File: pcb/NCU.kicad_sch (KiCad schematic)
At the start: 0 parts

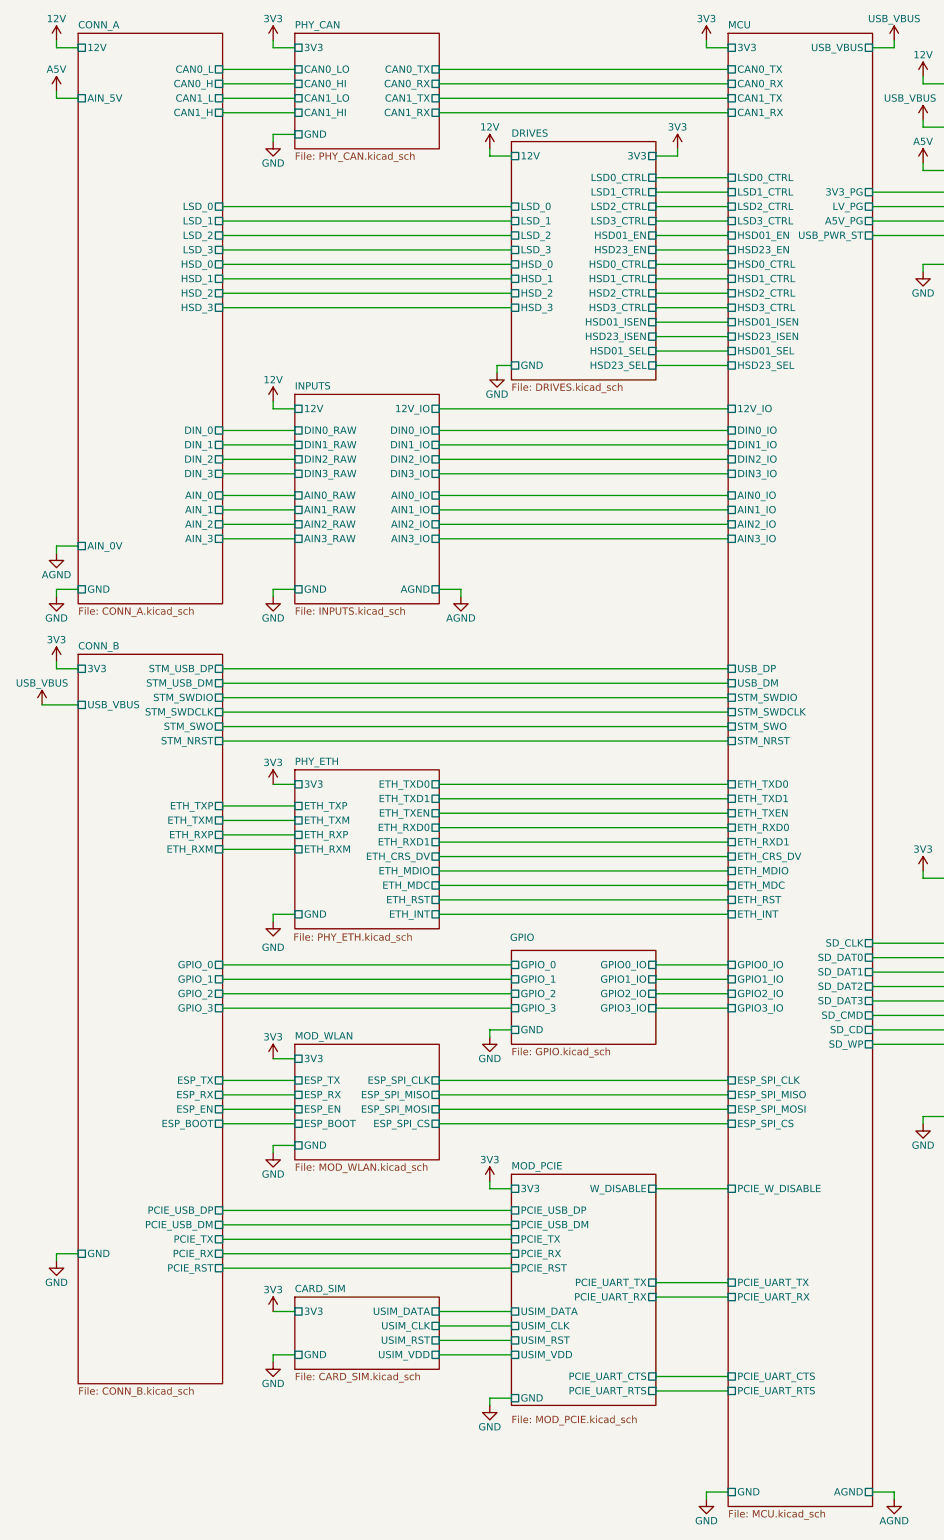
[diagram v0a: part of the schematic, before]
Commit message: added better lsds
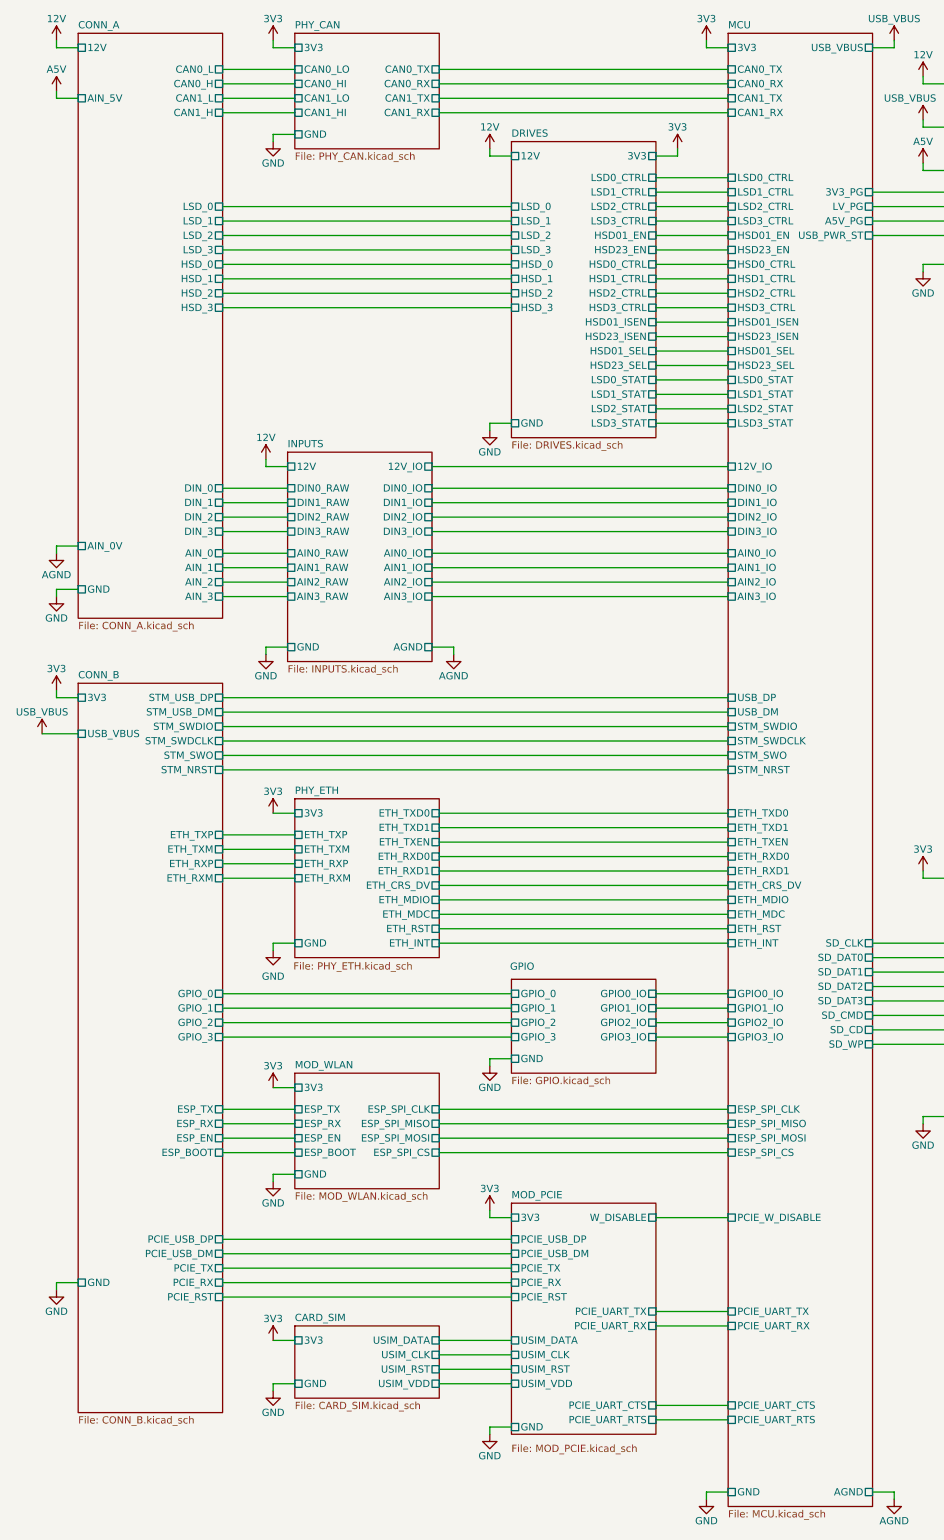
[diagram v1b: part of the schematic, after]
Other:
- sheet DRIVES ports: added LSD0_STAT, LSD1_STAT, LSD2_STAT, LSD3_STAT; removed none
- sheet MCU ports: added LSD0_STAT, LSD1_STAT, LSD2_STAT, LSD3_STAT; removed none

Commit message: power done
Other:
- sheet PWR ports: added 12V_PRT; removed none
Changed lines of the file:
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@@
 	(wire
 		(pts
+			(xy 208.28 26.67) (xy 208.28 27.94)
+		)
+		(stroke
+			(width 0)
+			(type default)
+		)
+	)
+	(wire
+		(pts
 			(xy 50.8 104.14) (xy 62.23 104.14)
 		)
@@
 	(wire
 		(pts
+			(xy 204.47 27.94) (xy 208.28 27.94)
+		)
+		(stroke
+			(width 0)
+			(type default)
+		)
+	)
+	(wire
+		(pts
 			(xy 165.1 52.07) (xy 177.8 52.07)
 		)
@@
 	(wire
 		(pts
-			(xy 204.47 27.94) (xy 208.28 27.94)
+			(xy 204.47 35.56) (xy 208.28 35.56)
 		)
 		(stroke
@@
 	(wire
 		(pts
-			(xy 208.28 26.67) (xy 208.28 27.94)
+			(xy 208.28 34.29) (xy 208.28 35.56)
 		)
 		(stroke
@@
 	(wire
 		(pts
-			(xy 204.47 35.56) (xy 208.28 35.56)
+			(xy 204.47 43.18) (xy 208.28 43.18)
 		)
 		(stroke
@@
 	(wire
 		(pts
-			(xy 208.28 34.29) (xy 208.28 35.56)
+			(xy 208.28 41.91) (xy 208.28 43.18)
 		)
 		(stroke
@@
 	(symbol
 		(lib_id "power:+12V")
-		(at 208.28 34.29 0)
+		(at 208.28 41.91 0)
 		(unit 1)
 		(exclude_from_sim no)
@@
 		(dnp no)
 		(property "Reference" "#PWR037"
-			(at 208.28 38.1 0)
+			(at 208.28 45.72 0)
 			(effects
 				(font
@@
 		)
 		(property "Value" "5V"
-			(at 208.28 30.48 0)
+			(at 208.28 38.1 0)
 			(effects
 				(font
@@
 		)
 		(property "Footprint" ""
-			(at 208.28 34.29 0)
+			(at 208.28 41.91 0)
 			(effects
 				(font
@@
 		)
 		(property "Datasheet" ""
-			(at 208.28 34.29 0)
+			(at 208.28 41.91 0)
 			(effects
 				(font
@@
 		)
 		(property "Description" "Power symbol creates a global label with name \"+12V\""
-			(at 208.28 34.29 0)
+			(at 208.28 41.91 0)
 			(effects
 				(font
@@
 			)
 		)
-		(property "Value" "12V"
+		(property "Value" "12V_PRT"
 			(at 97.79 35.56 0)
 			(effects
@@
 	(symbol
 		(lib_id "power:+12V")
+		(at 208.28 26.67 0)
+		(unit 1)
+		(exclude_from_sim no)
+		(in_bom yes)
+		(on_board yes)
+		(dnp no)
+		(property "Reference" "#PWR0346"
+			(at 208.28 30.48 0)
+			(effects
+				(font
+					(size 1.27 1.27)
+				)
+				(hide yes)
+			)
+		)
+		(property "Value" "12V_PRT"
+			(at 208.28 22.86 0)
+			(effects
+				(font
+					(size 1.27 1.27)
+				)
+			)
+		)
+		(property "Footprint" ""
+			(at 208.28 26.67 0)
+			(effects
+				(font
+					(size 1.27 1.27)
+				)
+				(hide yes)
+			)
+		)
+		(property "Datasheet" ""
+			(at 208.28 26.67 0)
+			(effects
+				(font
+					(size 1.27 1.27)
+				)
+				(hide yes)
+			)
+		)
+		(property "Description" "Power symbol creates a global label with name \"+12V\""
+			(at 208.28 26.67 0)
+			(effects
+				(font
+					(size 1.27 1.27)
+				)
+				(hide yes)
+			)
+		)
+		(pin "1"
+		)
+		(instances
+			(project "NCU"
+				(path "/3aee14c3-5480-4f7c-989e-3fef81779034"
+					(reference "#PWR0346")
+					(unit 1)
+				)
+			)
+		)
+	)
+	(symbol
+		(lib_id "power:+12V")
 		(at 58.42 93.98 0)
 		(unit 1)
@@
 			)
 		)
-		(property "Value" "12V"
+		(property "Value" "12V_PRT"
 			(at 58.42 90.17 0)
 			(effects
@@
 	(symbol
 		(lib_id "power:+12V")
-		(at 208.28 26.67 0)
+		(at 208.28 34.29 0)
 		(unit 1)
 		(exclude_from_sim no)
@@
 		(dnp no)
 		(property "Reference" "#PWR036"
-			(at 208.28 30.48 0)
+			(at 208.28 38.1 0)
 			(effects
 				(font
@@
 		)
 		(property "Value" "3V3"
-			(at 208.28 22.86 0)
+			(at 208.28 30.48 0)
 			(effects
 				(font
@@
 		)
 		(property "Footprint" ""
-			(at 208.28 26.67 0)
+			(at 208.28 34.29 0)
 			(effects
 				(font
@@
 		)
 		(property "Datasheet" ""
-			(at 208.28 26.67 0)
+			(at 208.28 34.29 0)
 			(effects
 				(font
@@
 		)
 		(property "Description" "Power symbol creates a global label with name \"+12V\""
-			(at 208.28 26.67 0)
+			(at 208.28 34.29 0)
 			(effects
 				(font
@@
 		)
 		(pin "3V3" passive
-			(at 204.47 27.94 0)
+			(at 204.47 35.56 0)
 			(effects
 				(font
@@
 		)
 		(pin "5V" passive
-			(at 204.47 35.56 0)
+			(at 204.47 43.18 0)
 			(effects
 				(font
@@
 			)
 		)
+		(pin "12V_PRT" passive
+			(at 204.47 27.94 0)
+			(effects
+				(font
+					(size 1.27 1.27)
+				)
+				(justify right)
+			)
+		)

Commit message: updated ethernet
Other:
- sheet GPIO ports: added 3V3; removed none
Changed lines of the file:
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@@
 	(wire
 		(pts
-			(xy 127 190.5) (xy 139.7 190.5)
+			(xy 127 194.31) (xy 139.7 194.31)
 		)
 		(stroke
@@
 	(wire
 		(pts
-			(xy 127 195.58) (xy 139.7 195.58)
+			(xy 127 199.39) (xy 139.7 199.39)
 		)
 		(stroke
@@
 	(wire
 		(pts
-			(xy 127 193.04) (xy 139.7 193.04)
+			(xy 127 196.85) (xy 139.7 196.85)
 		)
 		(stroke
@@
 	(wire
 		(pts
+			(xy 130.81 187.96) (xy 127 187.96)
+		)
+		(stroke
+			(width 0)
+			(type default)
+		)
+	)
+	(wire
+		(pts
 			(xy 127 54.61) (xy 139.7 54.61)
 		)
@@
 	(wire
 		(pts
-			(xy 127 187.96) (xy 139.7 187.96)
+			(xy 127 191.77) (xy 139.7 191.77)
 		)
 		(stroke
@@
 	)
 	(symbol
+		(lib_id "power:+12V")
+		(at 130.81 187.96 0)
+		(mirror y)
+		(unit 1)
+		(exclude_from_sim no)
+		(in_bom yes)
+		(on_board yes)
+		(dnp no)
+		(property "Reference" "#PWR0404"
+			(at 130.81 191.77 0)
+			(effects
+				(font
+					(size 1.27 1.27)
+				)
+				(hide yes)
+			)
+		)
+		(property "Value" "3V3"
+			(at 130.81 184.15 0)
+			(effects
+				(font
+					(size 1.27 1.27)
+				)
+			)
+		)
+		(property "Footprint" ""
+			(at 130.81 187.96 0)
+			(effects
+				(font
+					(size 1.27 1.27)
+				)
+				(hide yes)
+			)
+		)
+		(property "Datasheet" ""
+			(at 130.81 187.96 0)
+			(effects
+				(font
+					(size 1.27 1.27)
+				)
+				(hide yes)
+			)
+		)
+		(property "Description" "Power symbol creates a global label with name \"+12V\""
+			(at 130.81 187.96 0)
+			(effects
+				(font
+					(size 1.27 1.27)
+				)
+				(hide yes)
+			)
+		)
+		(pin "1"
+		)
+		(instances
+			(project "NCU"
+				(path "/3aee14c3-5480-4f7c-989e-3fef81779034"
+					(reference "#PWR0404")
+					(unit 1)
+				)
+			)
+		)
+	)
+	(symbol
 		(lib_id "power:GND")
 		(at 59.69 257.81 0)
@@
 		)
 		(pin "GPIO1_IO" passive
-			(at 127 190.5 0)
+			(at 127 194.31 0)
 			(effects
 				(font
@@
 		)
 		(pin "GPIO2_IO" passive
-			(at 127 193.04 0)
+			(at 127 196.85 0)
 			(effects
 				(font
@@
 		)
 		(pin "GPIO3_IO" passive
-			(at 127 195.58 0)
+			(at 127 199.39 0)
 			(effects
 				(font
@@
 		)
 		(pin "GPIO0_IO" passive
+			(at 127 191.77 0)
+			(effects
+				(font
+					(size 1.27 1.27)
+				)
+				(justify right)
+			)
+		)
+		(pin "3V3" passive
 			(at 127 187.96 0)
 			(effects
@@
 		)
 		(pin "GPIO2_IO" passive
-			(at 139.7 193.04 180)
+			(at 139.7 196.85 180)
 			(effects
 				(font
@@
 		)
 		(pin "GPIO1_IO" passive
-			(at 139.7 190.5 180)
+			(at 139.7 194.31 180)
 			(effects
 				(font
@@
 		)
 		(pin "GPIO3_IO" passive
-			(at 139.7 195.58 180)
+			(at 139.7 199.39 180)
 			(effects
 				(font
@@
 		)
 		(pin "GPIO0_IO" passive
-			(at 139.7 187.96 180)
+			(at 139.7 191.77 180)
 			(effects
 				(font

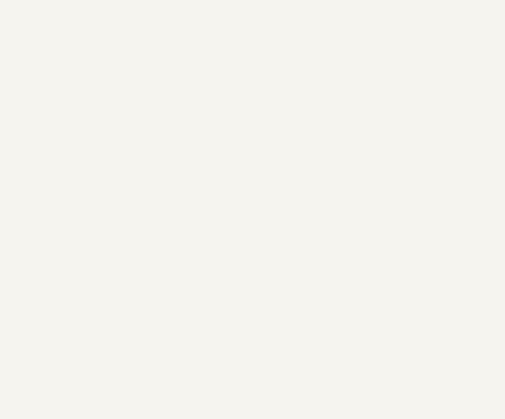
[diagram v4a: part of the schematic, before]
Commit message: initial layout of pcb with connectors, wlan and pcie modules
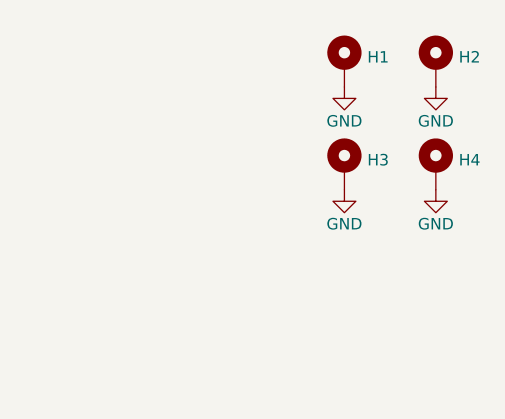
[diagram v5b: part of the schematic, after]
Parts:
- added H1, H2, H3, H4: MountingHole, MountingHole:MountingHole_3.2mm_M3_Pad, symbol Mechanical:MountingHole_Pad
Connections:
- net GND: now also H1.1, H2.1, H3.1, H4.1

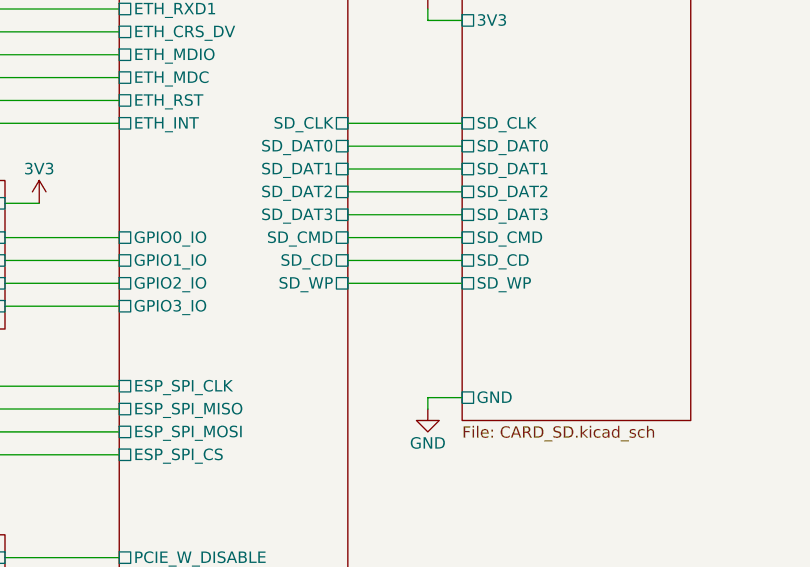
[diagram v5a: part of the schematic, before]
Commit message: sd card slot initial attempt (I meant SIM before)
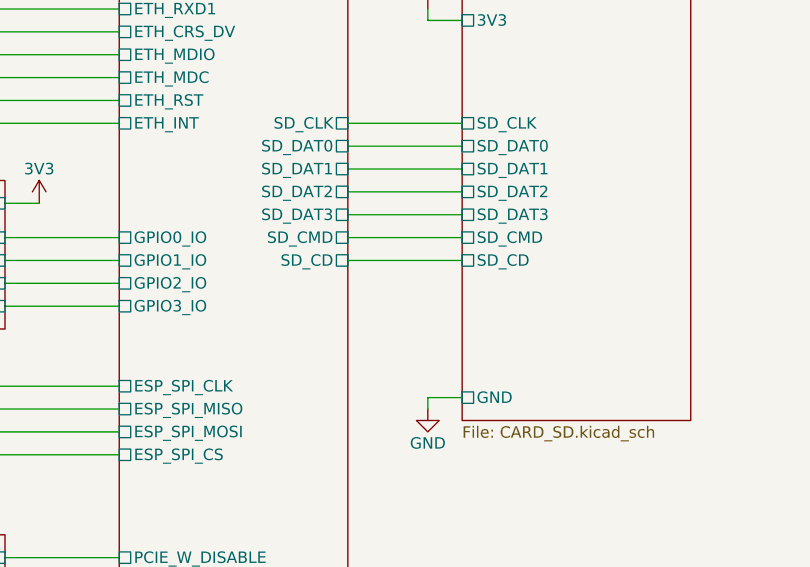
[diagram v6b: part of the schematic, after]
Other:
- sheet CARD_SD ports: added none; removed SD_WP
- sheet MCU ports: added none; removed SD_WP
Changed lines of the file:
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@@
 	(wire
 		(pts
-			(xy 165.1 196.85) (xy 177.8 196.85)
-		)
-		(stroke
-			(width 0)
-			(type default)
-		)
-	)
-	(wire
-		(pts
 			(xy 21.59 134.62) (xy 21.59 135.89)
 		)
@@
 			)
 		)
-		(pin "SD_WP" passive
-			(at 177.8 196.85 180)
-			(effects
-				(font
-					(size 1.27 1.27)
-				)
-				(justify left)
-			)
-		)
 		(pin "SD_DAT0" passive
 			(at 177.8 181.61 180)
@@
 			(effects
 				(font
-					(size 1.27 1.27)
-				)
-				(justify right)
-			)
-		)
-		(pin "SD_WP" passive
-			(at 165.1 196.85 0)
-			(effects
-				(font
